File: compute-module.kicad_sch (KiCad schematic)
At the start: 16 parts, among them J7 Conn_01x22_Female, SW1 SW_Push, SW2 SW_Push, U2 74154, U8 74LVC1G07SE-7

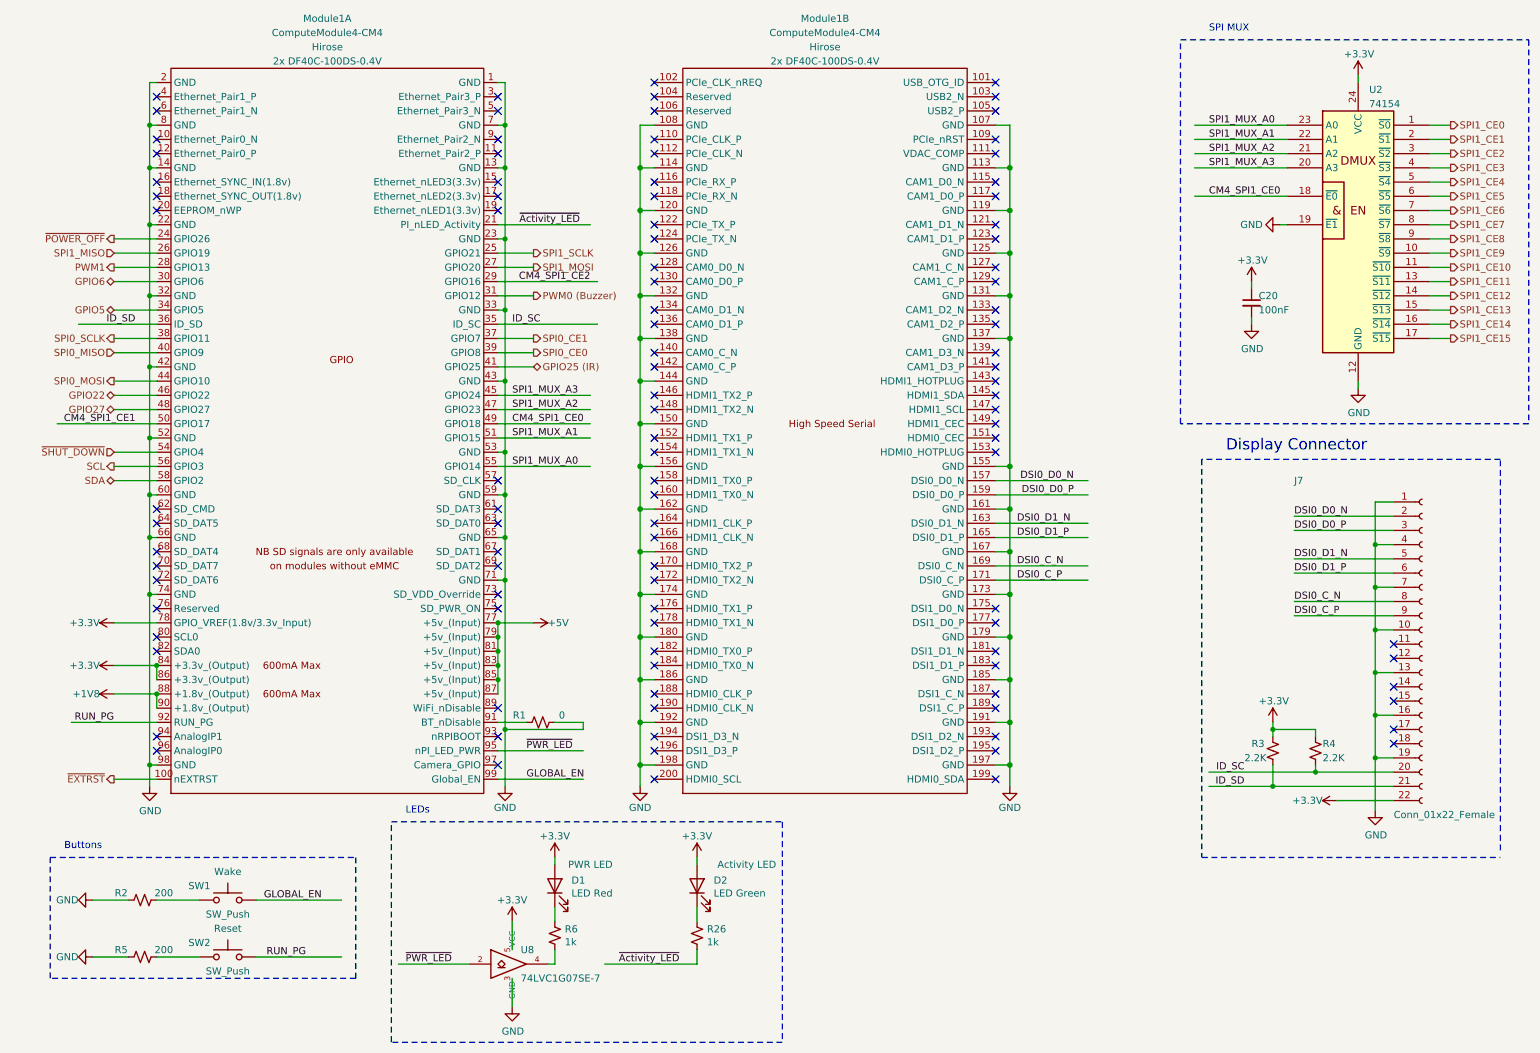
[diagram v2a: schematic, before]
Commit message: Finish connecting everything in sch.
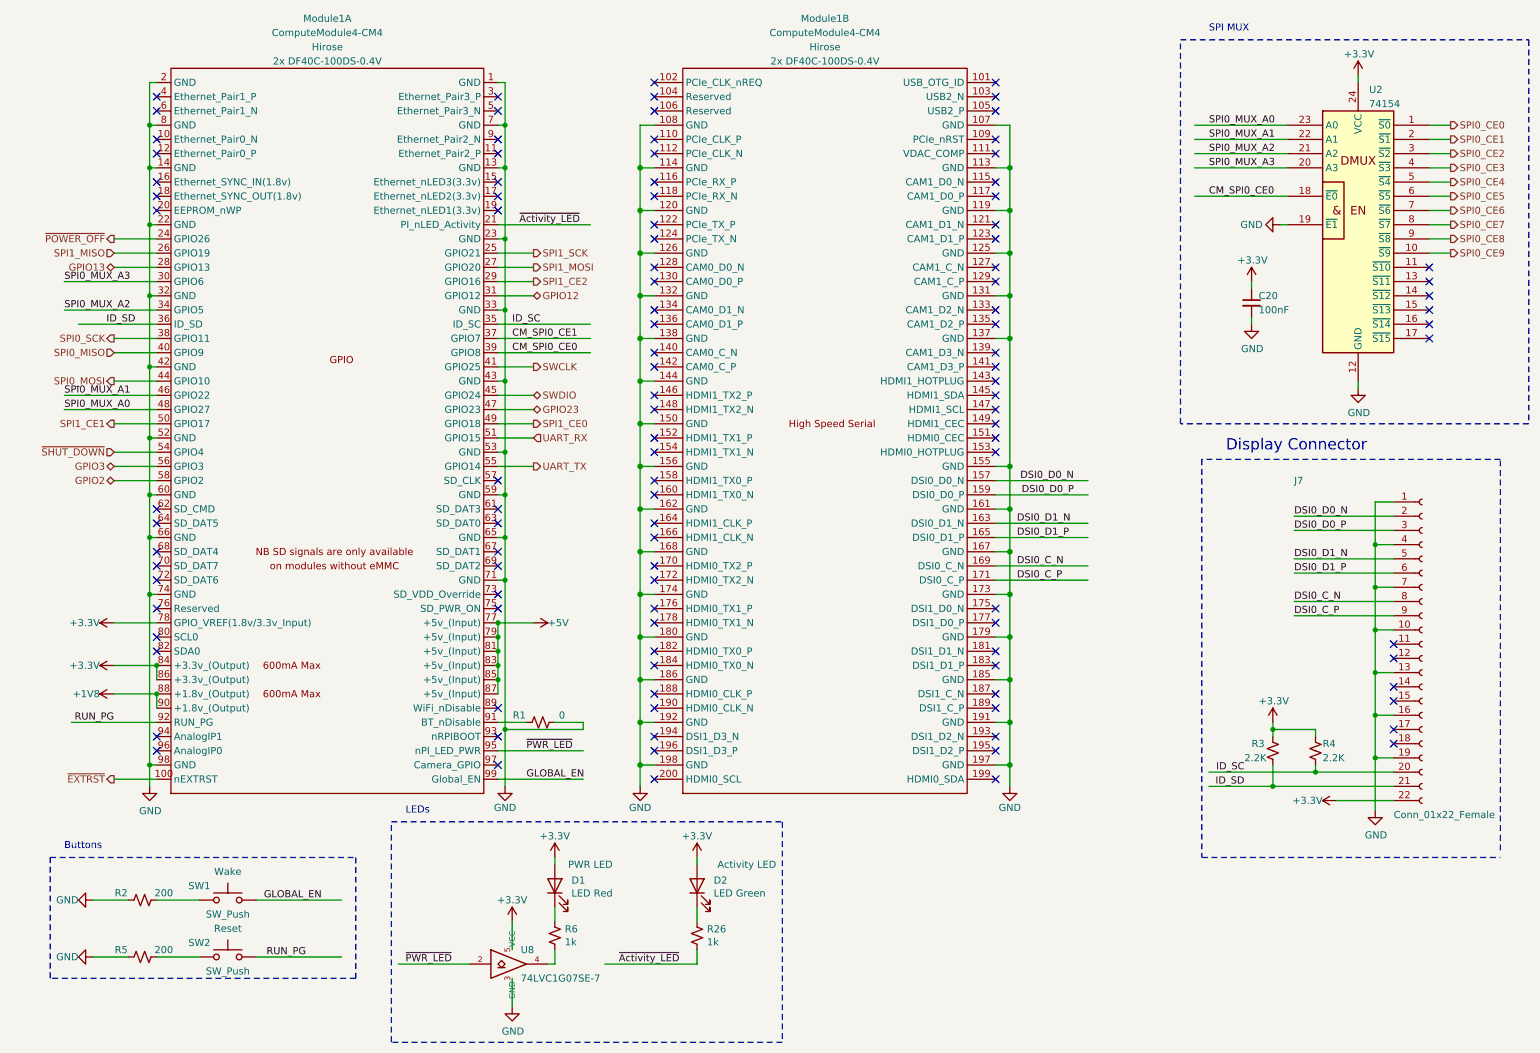
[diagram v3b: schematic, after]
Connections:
- net CM4_SPI1_CE1 is gone; now on net SPI1_CE1: Module1.50 (GPIO17)
- net CM4_SPI1_CE2 is gone; now on net SPI1_CE2: Module1.29 (GPIO16)
- net SPI0_CE0: now also U2.1 (~{S0}); no longer Module1.39 (GPIO8)
- net SPI0_CE1: now also U2.2 (~{S1}); no longer Module1.37 (GPIO7)
- net SPI1_CE0: now also Module1.49 (GPIO18); no longer U2.1 (~{S0})
- net SPI1_CE1: no longer U2.2 (~{S1})
- net SPI1_CE2: no longer U2.3 (~{S2})
- net CM4_SPI1_CE0 renamed CM_SPI0_CE0
- net CM_SPI0_CE0: now also Module1.39 (GPIO8); no longer Module1.49 (GPIO18)
- net GPIO22 renamed SPI0_MUX_A1
- net SPI0_MUX_A1: now also U2.22 (A1)
- net GPIO25 (IR) renamed SWCLK
- net GPIO27 renamed SPI0_MUX_A0
- net SPI0_MUX_A0: now also U2.23 (A0)
- net GPIO5 renamed SPI0_MUX_A2
- net SPI0_MUX_A2: now also U2.21 (A2)
- net GPIO6 renamed SPI0_MUX_A3
- net SPI0_MUX_A3: now also U2.20 (A3)
- net PWM0 (Buzzer) renamed GPIO12
- net PWM1 renamed GPIO13
- net SCL renamed GPIO3
- net SDA renamed GPIO2
- net SPI0_SCLK renamed SPI0_SCK
- net SPI1_CE10: no longer names the net of U2.11 (~{S10})
- net SPI1_CE11: no longer names the net of U2.13 (~{S11})
- net SPI1_CE12: no longer names the net of U2.14 (~{S12})
- net SPI1_CE13: no longer names the net of U2.15 (~{S13})
- net SPI1_CE14: no longer names the net of U2.16 (~{S14})
- net SPI1_CE15: no longer names the net of U2.17 (~{S15})
- net SPI1_CE3 renamed SPI0_CE3
- net SPI1_CE4 renamed SPI0_CE4
- net SPI1_CE5 renamed SPI0_CE5
- net SPI1_CE6 renamed SPI0_CE6
- net SPI1_CE7 renamed SPI0_CE7
- net SPI1_CE8 renamed SPI0_CE8
- net SPI1_CE9 renamed SPI0_CE9
- net SPI1_MUX_A0 renamed UART_TX
- net UART_TX: no longer U2.23 (A0)
- net SPI1_MUX_A1 renamed UART_RX
- net UART_RX: no longer U2.22 (A1)
- net SPI1_MUX_A2 renamed GPIO23
- net GPIO23: no longer U2.21 (A2)
- net SPI1_MUX_A3 renamed SWDIO
- net SWDIO: no longer U2.20 (A3)
- net SPI1_SCLK renamed SPI1_SCK
- new net CM_SPI0_CE1: Module1.37 (GPIO7)
- new net SPI0_CE2: U2.3 (~{S2})
- no-connect marks 104 -> 110

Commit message: Fix sch errors and warnings.
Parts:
- J7: value Conn_01x22_Female -> DSI; symbol Connector:Conn_01x22_Female -> Connector_Generic:Conn_01x22
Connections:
- no-connect marks 110 -> 111
